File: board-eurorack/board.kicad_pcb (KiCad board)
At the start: 2 copper layers, 20 x 108 mm, 64 parts, among them J1 Power, J10 B3, J12 C, J13 C1, J14 C2, J15 C3, J17 D, J18 D1, J19 D2, J2 A, J20 D3, J3 A1, J4 A2, J5 A3, J7 B, J8 B1, J9 B2, U1 OPA4197, U2 OPA4197, U4 OPA4197, U6 OPA4197

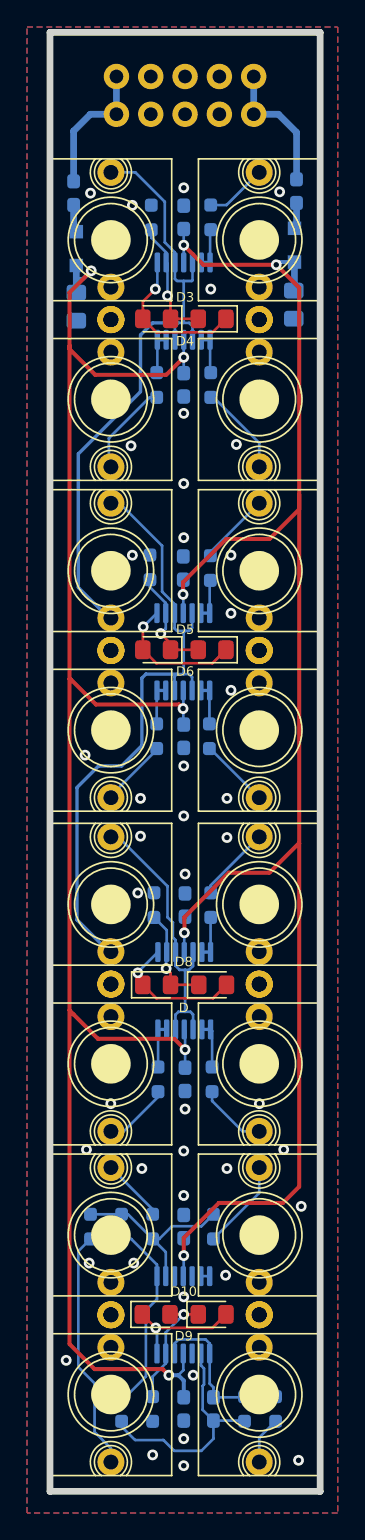
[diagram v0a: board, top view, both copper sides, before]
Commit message: Changes from tests on first revision
1. Silkscreen legibility changes
2. Added version numbers and such to page info blocks
3. Change MPNs and values
4. Change footprints for LEDs and Diodes.
5. Pin one markers
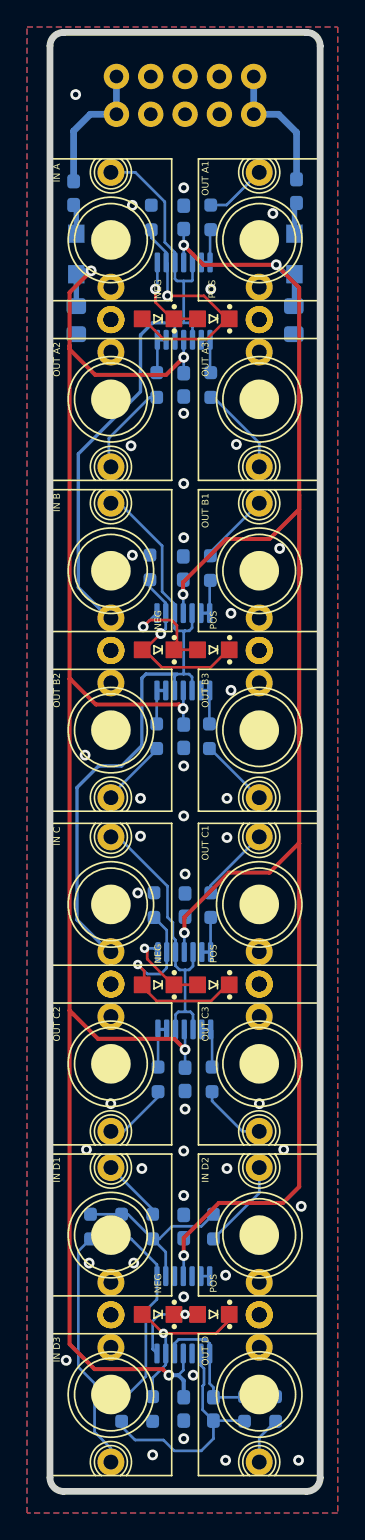
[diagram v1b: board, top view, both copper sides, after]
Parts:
- added G***: LOGO, winterbloom:Extra_Long_Wiggly_Boi_25mm, B.Cu at (106.4, 85.2)
- C11: value ??pF -> 12pF
- D1, D2: value 1N5819 -> BARRIER; footprint winterbloom:D_SOD-323_HandSoldering -> winterbloom:DIODE_SOD-123_SOD-123F
- D10, D3, D4, D5, D6, D8, D9: footprint LED_SMD:LED_0805_2012Metric_Pad1.15x1.40mm_HandSolder -> winterbloom:LED_0805_Kingbright_APT2012
- D7: renamed from D; footprint LED_SMD:LED_0805_2012Metric_Pad1.15x1.40mm_HandSolder -> winterbloom:LED_0805_Kingbright_APT2012
- FB1, FB2: value 300mA -> BEAD
- J10: value B3 -> OUT B3
- J12: value C -> IN C
- J13: value C1 -> OUT C1
- J14: value C2 -> OUT C2
- J15: value C3 -> OUT C3
- J17: value D -> OUT D
- J18: value D1 -> IN D1
- J19: value D2 -> IN D2
- J2: value A -> IN A
- J20: value D3 -> IN D3
- J3: value A1 -> OUT A1
- J4: value A2 -> OUT A2
- J5: value A3 -> OUT A3
- J7: value B -> IN B
- J8: value B1 -> OUT B1
- J9: value B2 -> OUT B2
- R1, R12, R13, R14, R2, R3, R5, R6, R7: value 100 -> 100R
- R10, R11, R16, R9: value 270 -> 270R
- U1, U2, U4, U6: value OPA4197 -> OPA4991
- moved D3 4.20 mm to (101.0, 69.2)
- moved D5 4.20 mm to (101.0, 93.7)
- moved D4 4.00 mm to (96.9, 69.2)
- moved D6 4.00 mm to (96.9, 93.7)
- moved C1 1.15 mm to (107.0, 69.2)
- moved C2 1.00 mm to (90.8, 69.2)
- moved D2 0.65 mm to (107.0, 64.3)
- moved D1 0.40 mm to (90.8, 64.3)
- moved D10 0.15 mm to (96.9, 142.8), turned to 180 degrees
- moved D8 0.10 mm to (96.9, 118.5), turned to 180 degrees
- moved D9 0.10 mm to (101.0, 142.8), turned to 180 degrees
- moved D7 0.06 mm to (101.0, 118.5), turned to 180 degrees
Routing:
- net Net-(D3-Pad1): track 9.23 -> 18.3 mm
- net Net-(D7-Pad1): track 7.62 -> 15.8 mm
- net Net-(D5-Pad1): track 8.60 -> 13.6 mm
- net Net-(D3-Pad2): track 11.6 -> 6.79 mm
- net Net-(D10-Pad2): track 9.14 -> 12.8 mm
- net Net-(D7-Pad2): track 10.2 -> 6.69 mm
- net Net-(D5-Pad2): track 10.1 -> 8.35 mm
- net Net-(D10-Pad1): track 8.95 -> 7.18 mm
- net +12V: track 126.5 -> 127.2 mm
- net Net-(D2-Pad2): track 1.72 -> 2.34 mm
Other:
- outline, holes or cut-outs redrawn
- board text added: "CERN-OHL-P V2 helium.wntr.dev"
- board text added: "Helium v2 10/2/2021"
- board text removed: "Winterbloom Helium v1 9/14/21 CERN-OHL-P V2"
